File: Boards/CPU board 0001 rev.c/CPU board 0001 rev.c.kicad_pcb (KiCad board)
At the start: 2 copper layers, 165.9 x 187.4 mm, 78 parts, among them J1 CEC card edge connector large, U1 SPARE, U10 7432, U11 7442, U12 7406, U13 7406, U14 7442, U15 7442, U16 M8216, U17 M8216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

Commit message: checked Rev.c cpu board and tweaked copper on a and b
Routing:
- net Net-(U14-0): track 93.4 -> 90.9 mm
- net Net-(U23-OEa): track 173.1 -> 171.8 mm, vias 3 -> 2
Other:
- board text added: "FAB NO. 07-0001 REV C"
- board text added: "SJC4A/94VO/14-82"
- board text removed: "FAB NO. 07-0001 REV A"
- board text removed: "PCB1 -5"
- board text removed: "original board repair"
- board text removed: "original mistake peeled up trace to fix"
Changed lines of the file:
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@@
   (gr_line (start 130.81 38.1) (end 127.635 41.91)
     (stroke (width 0.15) (type default)) (layer "F.SilkS"))
-  (gr_line (start 57.15 55.88) (end 56.515 55.245)
-    (stroke (width 0.15) (type default)) (layer "F.SilkS"))
-  (gr_line (start 56.515 55.245) (end 57.15 54.61)
-    (stroke (width 0.15) (type default)) (layer "F.SilkS"))
-  (gr_line (start 118.11 93.98) (end 114.3 90.805)
-    (stroke (width 0.15) (type default)) (layer "F.SilkS"))
-  (gr_line (start 56.515 55.245) (end 57.15 55.88)
-    (stroke (width 0.15) (type default)) (layer "F.SilkS"))
-  (gr_line (start 63.5 55.245) (end 56.515 55.245)
-    (stroke (width 0.15) (type default)) (layer "F.SilkS"))
-  (gr_line (start 64.77 56.515) (end 63.5 55.245)
-    (stroke (width 0.15) (type default)) (layer "F.SilkS"))
   (gr_line (start 130.175 41.91) (end 133.35 38.1)
-    (stroke (width 0.15) (type default)) (layer "F.SilkS"))
-  (gr_line (start 108.585 54.61) (end 108.585 50.8)
     (stroke (width 0.15) (type default)) (layer "F.SilkS"))
   (gr_line (start 41.78 187.67) (end 41.78 20.61)
@@
   (gr_line (start 51.93 10.46) (end 207.68 10.46)
     (stroke (width 0.1) (type default)) (layer "Edge.Cuts"))
+  (gr_text "SJC4A/94VO/14-82" (at 48.895 55.245 90) (layer "F.Cu")
+    (effects (font (size 1.5 1.5) (thickness 0.3) bold) (justify left bottom))
+  )
   (gr_text "61" (at 207.01 186.055 90) (layer "F.Cu")
     (effects (font (size 1.5 1.5) (thickness 0.3) bold) (justify left bottom))
@@
     (effects (font (size 1.5 1.5) (thickness 0.3) bold) (justify left bottom))
   )
-  (gr_text "FAB NO. 07-0001 REV A" (at 46.99 29.21 90) (layer "B.Cu")
+  (gr_text "FAB NO. 07-0001 REV C" (at 46.99 29.21 90) (layer "B.Cu")
     (effects (font (size 1.5 1.5) (thickness 0.3) bold) (justify left bottom mirror))
   )
@@
     (effects (font (size 1.5 1.5) (thickness 0.3) bold) (justify left bottom mirror))
   )
-  (gr_text "PCB1 -5" (at 50.8 29.21 90) (layer "B.Cu")
-    (effects (font (size 1.5 1.5) (thickness 0.3) bold) (justify left bottom mirror))
-  )
   (gr_text "122" (at 207.01 184.15 90) (layer "B.Cu")
     (effects (font (size 1.5 1.5) (thickness 0.3) bold) (justify left bottom mirror))
-  )
-  (gr_text "original board repair" (at 118.745 94.615) (layer "F.SilkS")
-    (effects (font (size 1 1) (thickness 0.15)) (justify left bottom))
   )
   (gr_text "PIZZA TIME\nTHEATER" (at 48.26 175.895 90) (layer "F.SilkS")
     (effects (font (size 1 1) (thickness 0.15)) (justify bottom))
   )
-  (gr_text "original mistake\npeeled up trace to fix" (at 107.315 57.785) (layer "F.SilkS")
-    (effects (font (size 1 1) (thickness 0.15)) (justify left bottom))
-  )
   (gr_text "ASSY NO. 06-0001" (at 46.355 50.8 90) (layer "F.SilkS")
-    (effects (font (size 1 1) (thickness 0.15)) (justify left bottom))
-  )
-  (gr_text "original board repair" (at 55.88 57.785) (layer "F.SilkS")
     (effects (font (size 1 1) (thickness 0.15)) (justify left bottom))
   )
@@
   (segment (start 72.39 107.95) (end 74.295 107.95) (width 1.27) (layer "F.Cu") (net 2))
   (segment (start 74.295 59.69) (end 74.295 48.26) (width 1.27) (layer "F.Cu") (net 2))
+  (segment (start 74.295 180.975) (end 74.295 185.42) (width 1.27) (layer "F.Cu") (net 2))
   (segment (start 122.55 180.965) (end 125.085 180.965) (width 1.27) (layer "F.Cu") (net 2))
   (segment (start 71.755 34.29) (end 71.755 16.51) (width 1.27) (layer "F.Cu") (net 2))
   (segment (start 207.645 91.44) (end 205.74 93.345) (width 1.27) (layer "F.Cu") (net 2))
-  (segment (start 76.815 187.94) (end 74.295 185.42) (width 1.27) (layer "F.Cu") (net 2))
   (segment (start 125.095 184.15) (end 125.095 180.975) (width 1.27) (layer "F.Cu") (net 2))
   (segment (start 192.405 13.97) (end 190.5 13.97) (width 1.27) (layer "F.Cu") (net 2))
@@
   (segment (start 214.63 60.96) (end 207.645 60.96) (width 1.27) (layer "F.Cu") (net 2))
   (segment (start 137.16 160.02) (end 135.255 160.02) (width 1.27) (layer "F.Cu") (net 2))
-  (segment (start 79.455 187.94) (end 76.815 187.94) (width 1.27) (layer "F.Cu") (net 2))
   (segment (start 117.475 124.46) (end 120.015 121.92) (width 1.27) (layer "F.Cu") (net 2))
   (segment (start 74.295 132.08) (end 74.295 132.715) (width 1.27) (layer "F.Cu") (net 2))
@@
   (segment (start 208.28 114.3) (end 214.63 114.3) (width 1.27) (layer "F.Cu") (net 2))
   (segment (start 93.98 12.7) (end 123.19 12.7) (width 1.27) (layer "F.Cu") (net 2))
-  (segment (start 74.295 185.42) (end 74.295 180.975) (width 1.27) (layer "F.Cu") (net 2))
   (segment (start 123.19 19.05) (end 123.19 12.7) (width 1.27) (layer "F.Cu") (net 2))
   (segment (start 130.81 36.83) (end 130.81 38.1) (width 1.27) (layer "F.Cu") (net 2))
@@
   (segment (start 214.63 91.44) (end 207.645 91.44) (width 1.27) (layer "F.Cu") (net 2))
   (segment (start 112.315 187.96) (end 121.285 187.96) (width 1.27) (layer "F.Cu") (net 2))
+  (segment (start 76.815 187.94) (end 79.455 187.94) (width 1.27) (layer "F.Cu") (net 2))
   (segment (start 207.01 115.57) (end 208.28 114.3) (width 1.27) (layer "F.Cu") (net 2))
   (segment (start 187.325 57.15) (end 187.325 25.4) (width 1.27) (layer "F.Cu") (net 2))
@@
   (segment (start 100.33 83.82) (end 100.33 72.39) (width 1.27) (layer "F.Cu") (net 2))
   (segment (start 166.37 104.14) (end 167.64 102.87) (width 0.4) (layer "F.Cu") (net 2))
+  (segment (start 74.295 185.42) (end 76.815 187.94) (width 1.27) (layer "F.Cu") (net 2))
   (segment (start 182.245 107.95) (end 182.245 65.405) (width 1.27) (layer "F.Cu") (net 2))
   (segment (start 125.095 59.69) (end 127.635 59.69) (width 1.27) (layer "F.Cu") (net 2))
@@
   (segment (start 138.43 15.24) (end 137.795 14.605) (width 0.4) (layer "B.Cu") (net 138))
   (segment (start 116.205 133.985) (end 116.205 104.14) (width 0.4) (layer "F.Cu") (net 139))
+  (segment (start 113.665 88.9) (end 117.475 92.71) (width 0.4) (layer "F.Cu") (net 139))
   (segment (start 107.315 59.69) (end 107.315 66.04) (width 0.4) (layer "F.Cu") (net 139))
-  (segment (start 117.475 93.98) (end 113.665 90.17) (width 0.4) (layer "F.Cu") (net 139))
   (segment (start 108.585 78.74) (end 107.315 80.01) (width 0.4) (layer "F.Cu") (net 139))
   (segment (start 107.315 66.04) (end 108.585 67.31) (width 0.4) (layer "F.Cu") (net 139))
   (segment (start 116.205 104.14) (end 117.475 102.87) (width 0.4) (layer "F.Cu") (net 139))
-  (segment (start 117.475 100.33) (end 117.475 97.79) (width 0.4) (layer "F.Cu") (net 139))
-  (segment (start 117.475 97.79) (end 117.475 95.25) (width 0.4) (layer "F.Cu") (net 139))
-  (segment (start 117.475 97.79) (end 117.475 93.98) (width 0.4) (layer "F.Cu") (net 139))
   (segment (start 108.585 67.31) (end 108.585 78.74) (width 0.4) (layer "F.Cu") (net 139))
+  (segment (start 117.475 92.71) (end 117.475 100.33) (width 0.4) (layer "F.Cu") (net 139))
   (segment (start 117.475 102.87) (end 117.475 100.33) (width 0.4) (layer "F.Cu") (net 139))
-  (segment (start 113.665 90.17) (end 113.665 88.9) (width 0.4) (layer "F.Cu") (net 139))
   (segment (start 107.315 80.01) (end 107.315 83.82) (width 0.4) (layer "F.Cu") (net 139))
   (via (at 113.665 88.9) (size 0.8) (drill 0.4) (layers "F.Cu" "B.Cu") (net 139))
@@
   (segment (start 138.325 82.02) (end 136.525 83.82) (width 0.4) (layer "B.Cu") (net 147))
   (segment (start 139.7 52.07) (end 139.7 49.53) (width 0.4) (layer "F.Cu") (net 148))
-  (segment (start 55.88 55.88) (end 55.88 52.07) (width 0.4) (layer "F.Cu") (net 148))
+  (segment (start 57.15 52.07) (end 57.15 54.61) (width 0.4) (layer "F.Cu") (net 148))
   (segment (start 137.16 54.61) (end 139.7 52.07) (width 0.4) (layer "F.Cu") (net 148))
+  (segment (start 54.61 57.15) (end 54.61 59.69) (width 0.4) (layer "F.Cu") (net 148))
+  (segment (start 57.15 54.61) (end 54.61 57.15) (width 0.4) (layer "F.Cu") (net 148))
   (segment (start 170.18 50.8) (end 170.18 49.53) (width 0.4) (layer "F.Cu") (net 148))
-  (segment (start 54.61 59.69) (end 54.61 57.15) (width 0.4) (layer "F.Cu") (net 148))
   (segment (start 167.64 53.34) (end 170.18 50.8) (width 0.4) (layer "F.Cu") (net 148))
-  (segment (start 55.88 48.895) (end 57.15 47.625) (width 0.4) (layer "F.Cu") (net 148))
-  (segment (start 55.88 52.07) (end 55.88 48.895) (width 0.4) (layer "F.Cu") (net 148))
-  (segment (start 57.15 47.625) (end 57.15 34.29) (width 0.4) (layer "F.Cu") (net 148))
-  (segment (start 54.61 57.15) (end 55.88 55.88) (width 0.4) (layer "F.Cu") (net 148))
+  (segment (start 57.15 34.29) (end 57.15 52.07) (width 0.4) (layer "F.Cu") (net 148))
   (segment (start 137.16 57.15) (end 137.16 54.61) (width 0.4) (layer "F.Cu") (net 148))
-  (segment (start 57.15 52.07) (end 55.88 52.07) (width 0.4) (layer "F.Cu") (net 148))
   (segment (start 167.64 57.15) (end 167.64 53.34) (width 0.4) (layer "F.Cu") (net 148))
   (segment (start 161.925 49.53) (end 161.925 57.15) (width 0.4) (layer "F.Cu") (net 148))
   (via (at 161.925 49.53) (size 0.8) (drill 0.4) (layers "F.Cu" "B.Cu") (net 148))
   (via (at 161.925 57.15) (size 0.8) (drill 0.4) (layers "F.Cu" "B.Cu") (net 148))
-  (via (at 108.585 50.165) (size 0.8) (drill 0.4) (layers "F.Cu" "B.Cu") (net 148))
   (segment (start 132.08 47.625) (end 132.715 46.99) (width 0.4) (layer "B.Cu") (net 148))
   (segment (start 158.75 50.8) (end 160.02 49.53) (width 0.4) (layer "B.Cu") (net 148))

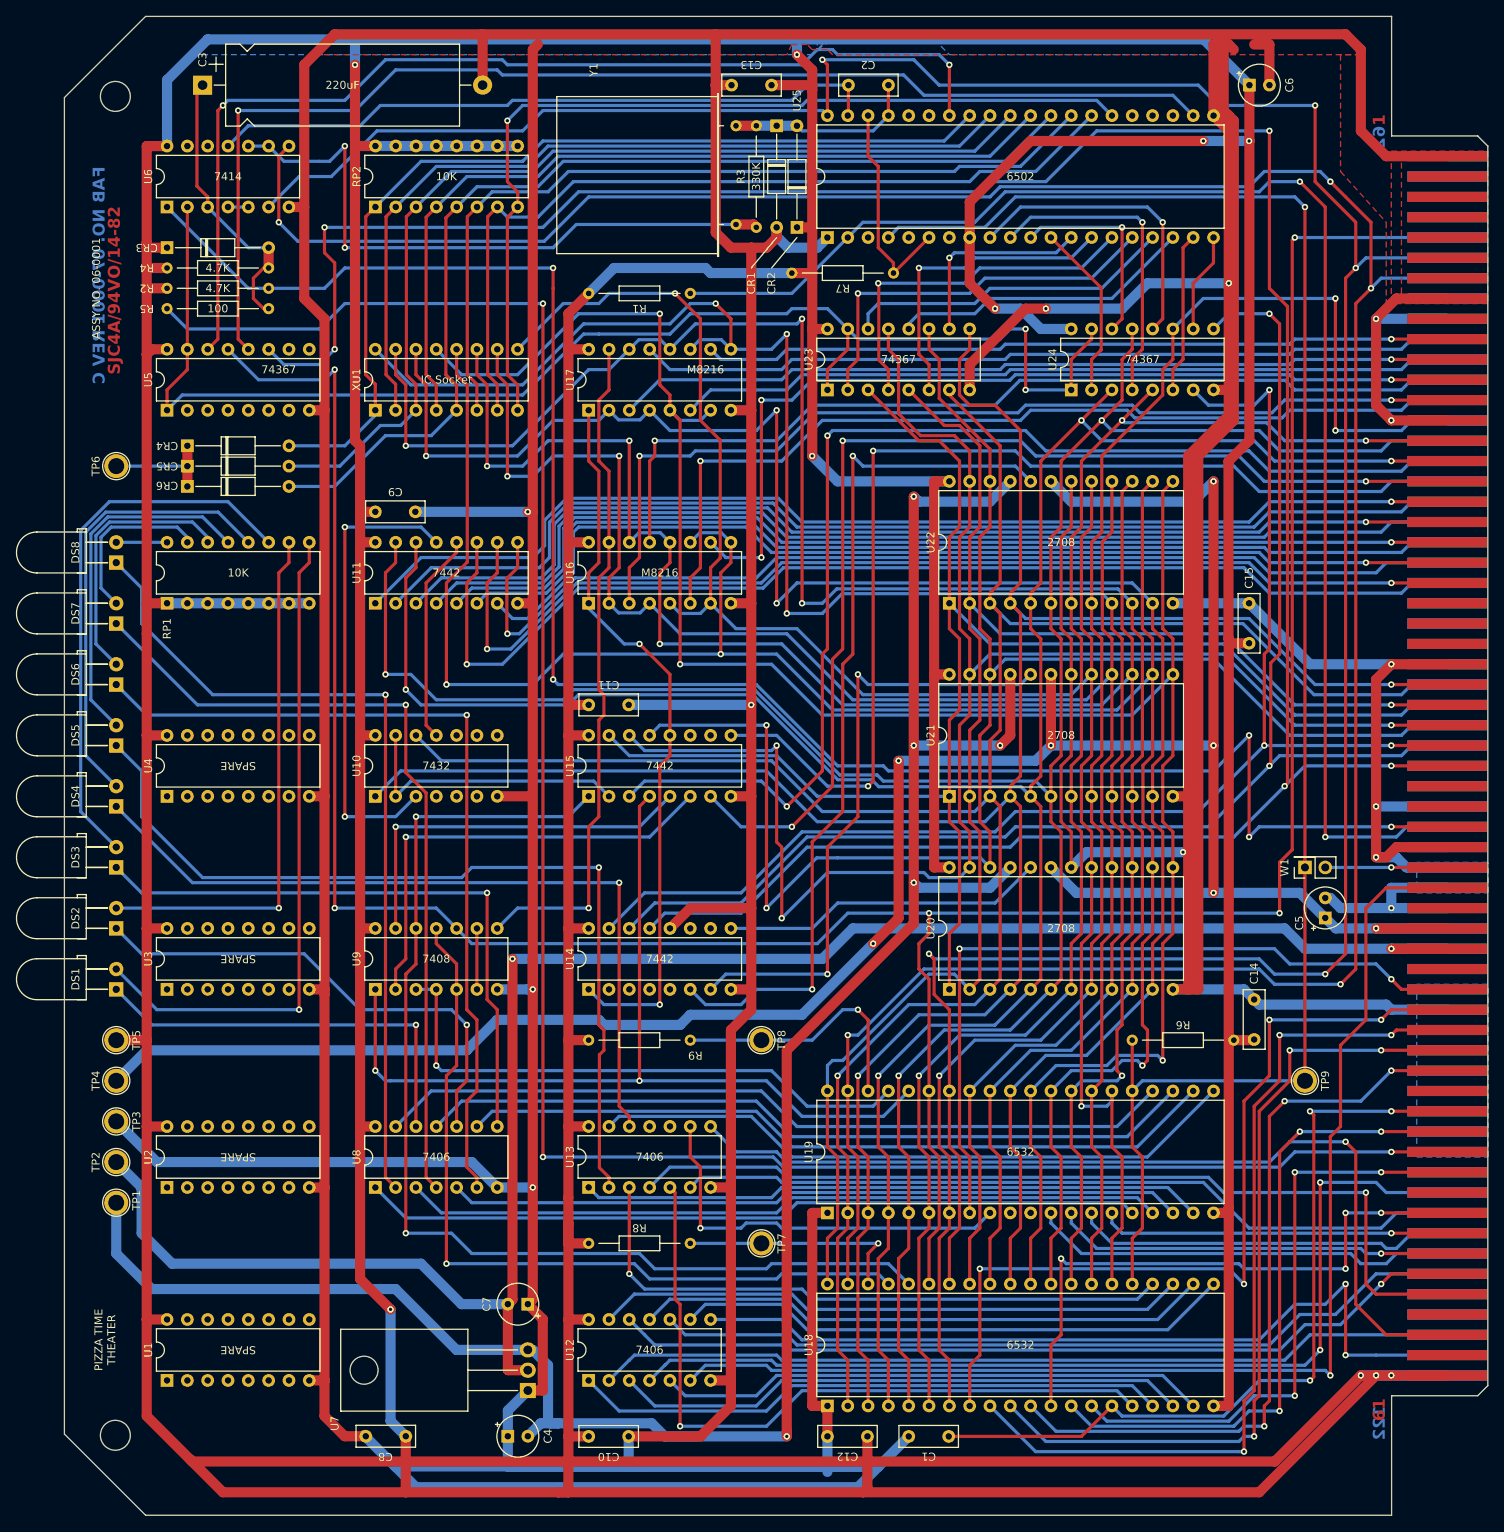
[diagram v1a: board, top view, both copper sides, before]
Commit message: updated boards per real one
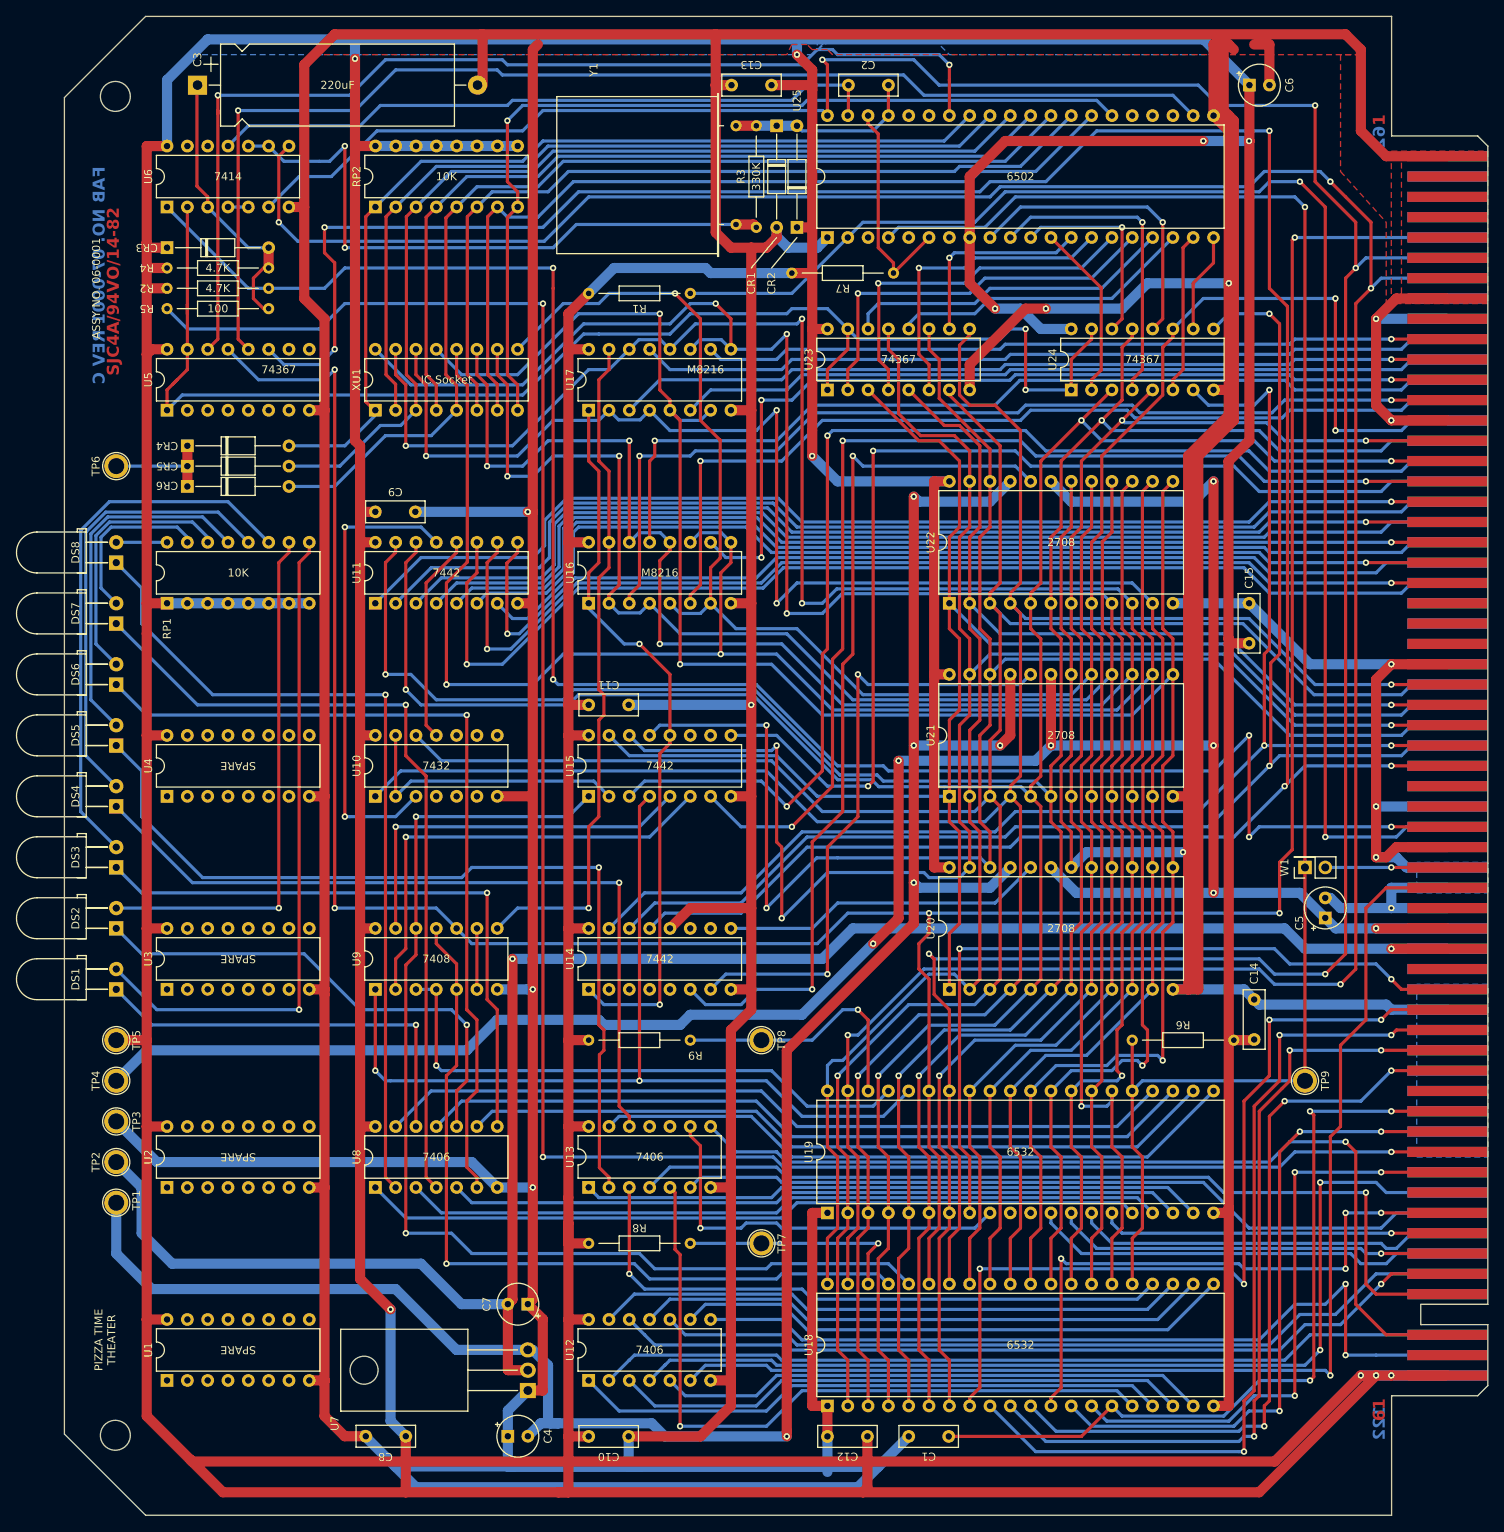
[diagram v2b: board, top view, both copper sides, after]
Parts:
- moved C3 0.63 mm to (58.4, 19.1)
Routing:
- net Net-(U23-OEa): track 171.8 -> 173.7 mm
- net +5V: track 1497.0 -> 1498.9 mm
- net cpu R/~{W}: track 132.6 -> 134.1 mm
- net Net-(CR3-A): track 35.8 -> 34.8 mm

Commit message: revisions from real life boards
tip130a is actually tip30a, widened holes for crystal, widened holes for big power resistor, fixed cpu board LED resistors
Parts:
- RP1: value 10K -> 330
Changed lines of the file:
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@@
         (effects (font (size 1 1) (thickness 0.15)))
     )
-    (fp_text value "10K" (at 3.81 8.89 180) (layer "F.SilkS")
+    (fp_text value "330" (at 3.81 8.89 180) (layer "F.SilkS")
         (effects (font (size 1 1) (thickness 0.15)))
     )
@@
     (fp_line (start 16.135 2.5) (end -3.795 2.5)
       (stroke (width 0.1) (type solid)) (layer "F.Fab"))
-    (pad "1" thru_hole circle (at 0 0 270) (size 1.4 1.4) (drill 0.7) (layers "*.Cu" "*.Mask")
+    (pad "1" thru_hole circle (at 0 0 270) (size 2 2) (drill 1) (layers "*.Cu" "*.Mask")
       (net 8 "Net-(CR1-K)") (pinfunction "1") (pintype "passive"))
-    (pad "2" thru_hole circle (at 12.34 0 270) (size 1.4 1.4) (drill 0.7) (layers "*.Cu" "*.Mask")
+    (pad "2" thru_hole circle (at 12.34 0 270) (size 2 2) (drill 1) (layers "*.Cu" "*.Mask")
       (net 114 "Net-(R3-Pad1)") (pinfunction "2") (pintype "passive"))
     (model "${KICAD6_3DMODEL_DIR}/Crystal.3dshapes/Crystal_HC33-U_Horizontal.wrl"
